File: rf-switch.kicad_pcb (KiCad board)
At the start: 2 copper layers, 1 part

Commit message: Started PCB Layout
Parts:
- removed RFS1: ~, PE42440_rf_switch:PE42440
- added C1: 0.01u, Capacitor_SMD:C_1206_3216Metric, F.Cu at (143.3, 106.7)
- added C2: 0.01u, Capacitor_SMD:C_1206_3216Metric, F.Cu at (143.3, 112.3)
- added C3: 10u, Capacitor_SMD:C_1206_3216Metric, F.Cu at (149.7, 106.7)
- added C4: 0.01u, Capacitor_SMD:C_1206_3216Metric, F.Cu at (149.7, 112.2)
- added C5: 0.01u, Capacitor_SMD:C_1206_3216Metric, F.Cu at (156.4, 106.5)
- added IC1: PE42440MLBB-Z, PE42440_rf_switch:PE42440, F.Cu at (155.8, 94.6)
- added J1: Conn_01x04_Pin, Connector_PinHeader_2.54mm:PinHeader_1x04_P2.54mm_Vertical, F.Cu at (170.8, 105.8)
- added J2: Conn_Coaxial_Small, Connector_Coaxial:SMA_Amphenol_132289_EdgeMount, F.Cu at (156.7, 65.8)
- added J3: Conn_Coaxial_Small, Connector_Coaxial:SMA_Amphenol_132289_EdgeMount, F.Cu at (197.3, 81.5)
- added J4: Conn_Coaxial_Small, Connector_Coaxial:SMA_Amphenol_132289_EdgeMount, F.Cu at (100.0, 75.0)
- added J5: Conn_Coaxial_Small, Connector_Coaxial:SMA_Amphenol_132289_EdgeMount, F.Cu at (100.0, 100.0)
- added J6: Conn_Coaxial_Small, Connector_Coaxial:SMA_Amphenol_132289_EdgeMount, F.Cu at (197.3, 104.9)
- added R1: 1M, Resistor_SMD:R_1206_3216Metric, F.Cu at (156.6, 112.4)
- added R2: 1M, Resistor_SMD:R_1206_3216Metric, F.Cu at (163.3, 106.6)
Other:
- board outline added: 100 x 65 mm

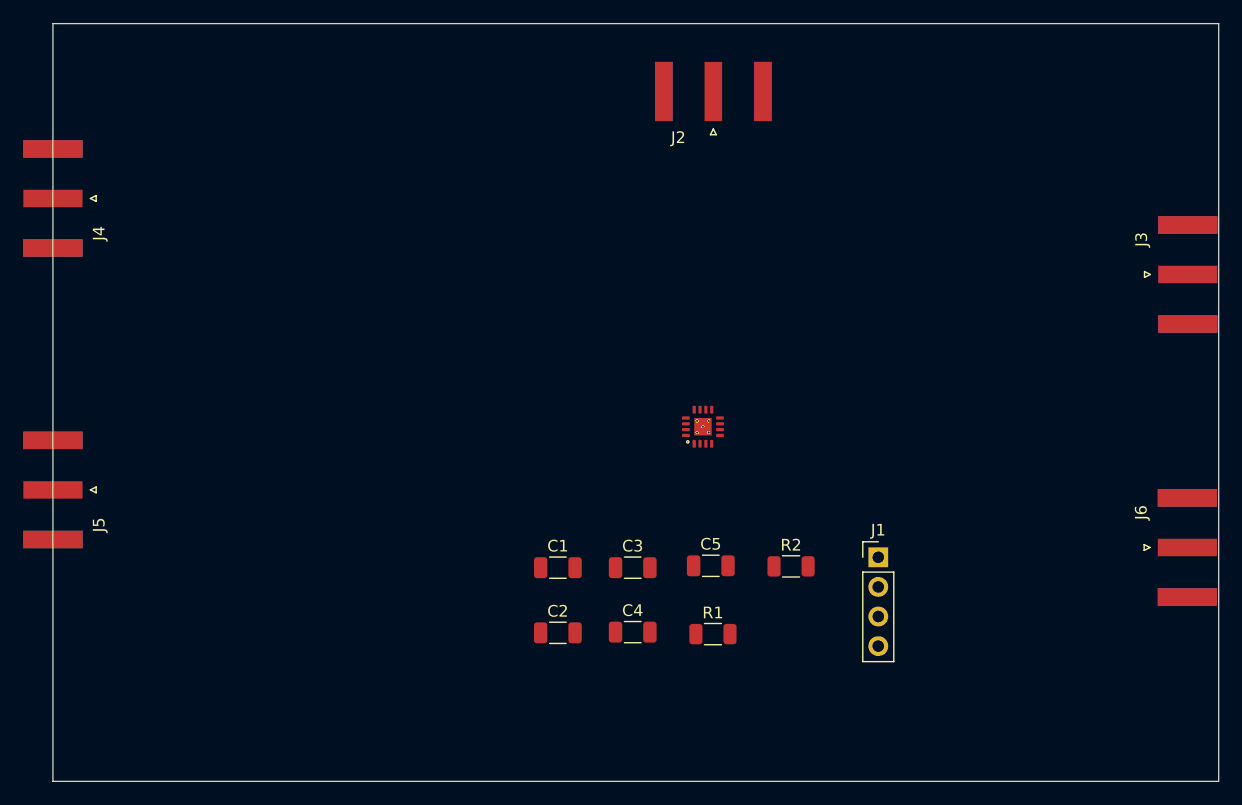
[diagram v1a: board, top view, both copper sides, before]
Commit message: Semi-completed PCB Schematic
Done wiring some of the components. Still need to finish this.
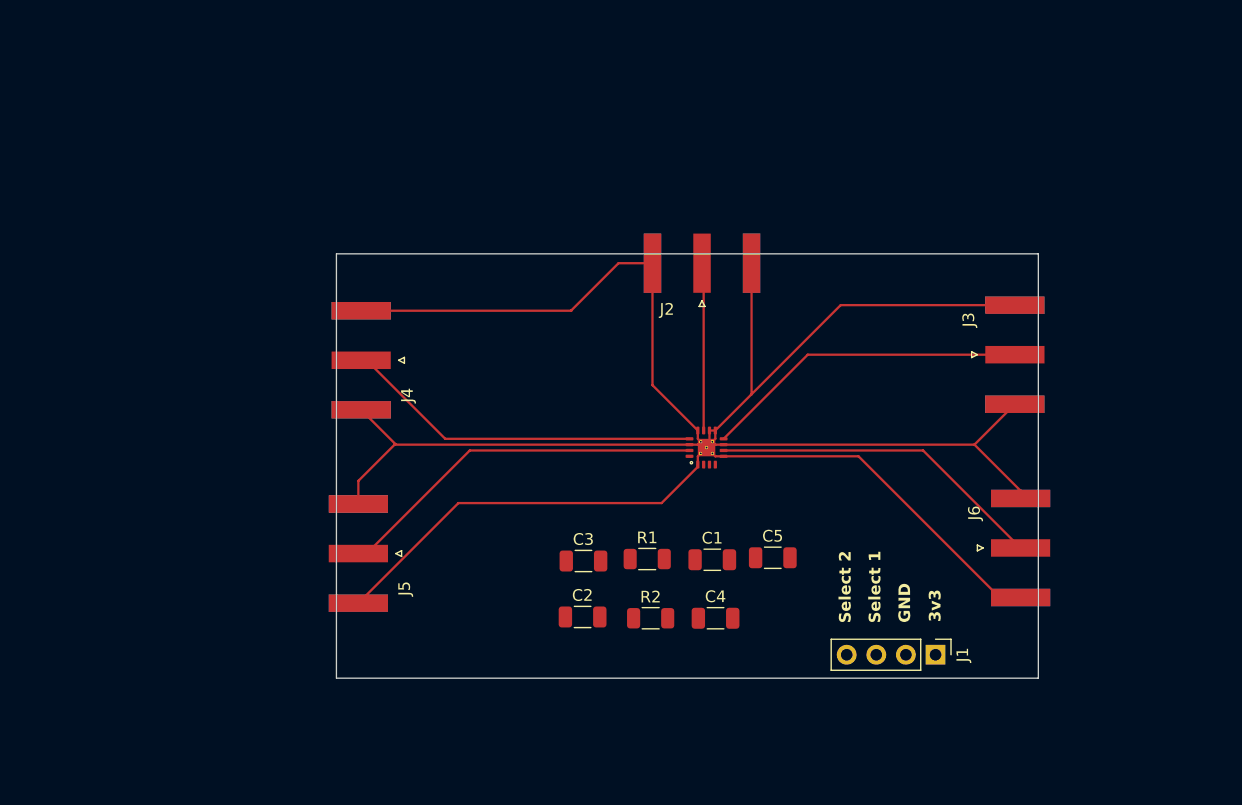
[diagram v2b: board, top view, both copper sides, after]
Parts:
- moved J4 29.9 mm to (126.4, 88.9)
- moved J5 26.8 mm to (126.2, 105.5)
- moved J3 16.3 mm to (182.5, 88.4)
- moved J2 14.8 mm to (155.7, 80.6)
- moved J6 14.3 mm to (183.0, 105.0)
- moved C1 13.3 mm to (156.6, 106.0)
- moved R2 12.8 mm to (151.3, 111.0)
- moved J1 9.70 mm to (175.7, 114.1), turned to -90 degrees
- moved R1 8.56 mm to (151.0, 105.9)
- moved C4 7.20 mm to (156.8, 111.0)
- moved C5 5.36 mm to (161.8, 105.8)
- moved C3 4.26 mm to (145.5, 106.1)
- moved C2 2.52 mm to (145.4, 110.9)
- moved IC1 1.81 mm to (156.1, 96.4)
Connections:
- C4 pad 1: /GND_1 -> GND
- IC1 pad 1: /GND_1 -> GND
- J4 pad 1: GND -> Net-(IC1-RF1)
- J4 pad 2: Net-(IC1-RF1) -> GND
- J5 pad 1: GND -> Net-(IC1-RF2)
- J5 pad 2: Net-(IC1-RF2) -> GND
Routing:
- net GND: track 0.00 -> 226.9 mm
- net Net-(IC1-RF2): track 0.00 -> 31.4 mm
- net Net-(IC1-RF1): track 0.00 -> 30.5 mm
- net Net-(IC1-RF4): track 0.00 -> 28.9 mm
- net Net-(IC1-RF3): track 0.00 -> 28.0 mm
- net Net-(IC1-RFC): track 0.00 -> 14.4 mm
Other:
- board size 100 x 65 mm -> 60.2 x 36.4 mm
- board text added: "3v3"
- board text added: "GND"
- board text added: "Select 1"
- board text added: "Select 2"

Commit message: PCB layout is done
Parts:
- removed C5: 0.01u, Capacitor_SMD:C_1206_3216Metric
- C2: value 0.01u -> 10u
- C3: value 10u -> 0.01u
- R1, R2: value 1M -> 10k
- moved R2 20.5 mm to (169.4, 101.5), turned to -90 degrees
- moved J1 17.6 mm to (158.1, 114.3), turned to 90 degrees
- moved J5 16.4 mm to (142.6, 105.5)
- moved J4 15.9 mm to (142.3, 88.8)
- moved C3 14.3 mm to (159.1, 101.6), turned to -90 degrees
- moved C4 13.3 mm to (166.2, 101.5), turned to -90 degrees
- moved R1 12.4 mm to (162.6, 101.5), turned to -90 degrees
- moved C2 11.3 mm to (156.0, 106.9), turned to -90 degrees
- moved J6 8.25 mm to (174.8, 105.0)
- moved J3 8.15 mm to (174.4, 88.4)
- moved C1 4.47 mm to (155.9, 101.6), turned to -90 degrees
- moved J2 3.25 mm to (155.8, 83.8)
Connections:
- C1 pad 1: /Select_2 -> Net-(IC1-VDD)
- C1 pad 2: GND -> Net-(C1-Pad2)
- C2 pad 1: /Select_1 -> Net-(C1-Pad2)
- C2 pad 2: GND -> /3v3
- C3 pad 1: Net-(C3-Pad1) -> /Select_2
- C4 pad 1: GND -> /Select_1
- IC1 pad 2: /3v3 -> Net-(IC1-VDD)
- R1 pad 1: Net-(C3-Pad1) -> /Select_2
- R1 pad 2: /Select_2 -> GND
- R2 pad 1: Net-(C3-Pad1) -> /Select_1
- R2 pad 2: /Select_1 -> GND
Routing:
- net GND: track 226.9 -> 11.2 mm, vias 0 -> 39
- net /Select_1: track 0.00 -> 29.3 mm
- net /Select_2: track 0.00 -> 23.3 mm
- net Net-(IC1-RF2): track 31.4 -> 15.7 mm
- net Net-(IC1-RF1): track 30.5 -> 15.1 mm
- net Net-(IC1-RF3): track 28.0 -> 19.8 mm
- net /3v3: track 0.00 -> 6.74 mm
- net Net-(IC1-RF4): track 28.9 -> 22.2 mm
- net Net-(IC1-RFC): track 14.4 -> 11.1 mm
- net Net-(C1-Pad2): track 0.00 -> 2.43 mm
- net Net-(IC1-VDD): track 0.00 -> 2.30 mm
- added copper zone on B.Cu, net GND
- added copper zone on F.Cu, net GND
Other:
- board size 60.2 x 36.4 mm -> 34.2 x 34.2 mm
- board text added: "S1"
- board text added: "S2"
- board text removed: "Select 1"
- board text removed: "Select 2"
